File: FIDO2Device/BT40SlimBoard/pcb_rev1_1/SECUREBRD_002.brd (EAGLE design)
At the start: 30 x 30 mm, 31 parts, among them CN1 USB4105-GF-A, CN2 IF_5PIN_H, CN3 IF_2PIN_SOL, SW1 SKRPACE010, SW2 SKRPACE010, SW3 SKTADAE010, U1 BT40, U2 ADP122ACPZ-3.3-R7

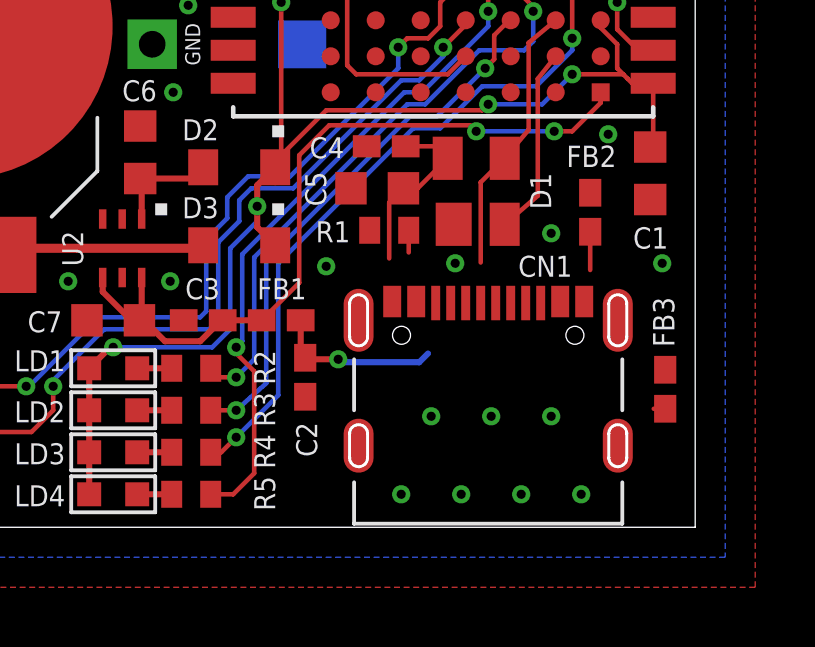
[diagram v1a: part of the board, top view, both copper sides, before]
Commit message: 配線レイアウトを修正
・部品入れ替えに伴い、配線レイアウトを修正
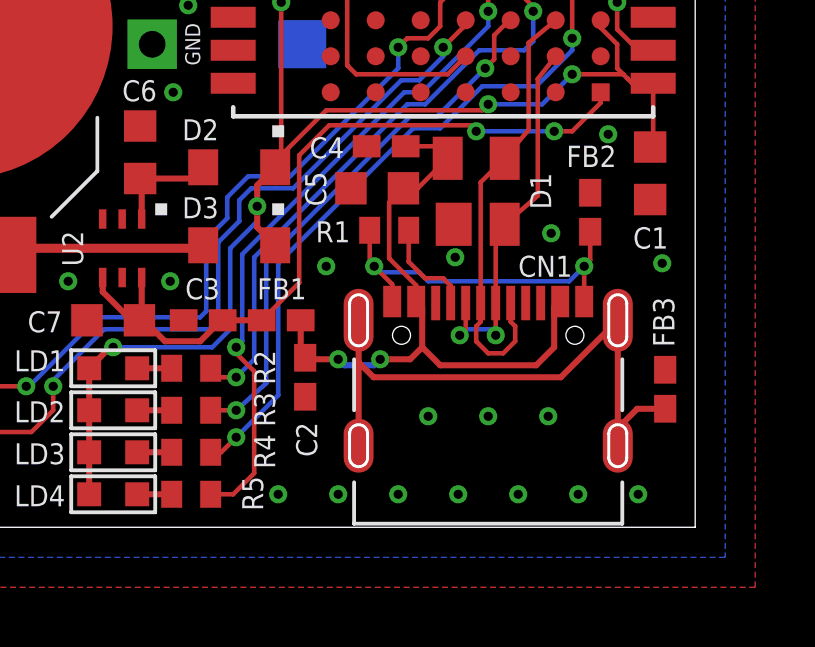
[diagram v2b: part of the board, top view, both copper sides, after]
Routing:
- net FG: track 0.38 -> 19.9 mm
- net USB_GND: track 1.27 -> 12.5 mm, vias 0 -> 2
- net VBUS: track 11.6 -> 21.6 mm, vias 1 -> 2
- net D_N: track 6.32 -> 12.7 mm, vias 0 -> 2
- net D_P: track 9.12 -> 14.8 mm
- net N$2: track 0.74 -> 3.36 mm
- net 0V: vias 18 -> 21
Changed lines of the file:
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@@
 </element>
 <element name="R5" library="Parts" package="R0402" value="390" x="13.2" y="1.1" smashed="yes" rot="R180">
-<attribute name="NAME" x="15.3" y="1.7" size="0.7" layer="25" rot="R270"/>
+<attribute name="NAME" x="14.9" y="1.7" size="0.7" layer="25" rot="R270"/>
 <attribute name="VALUE" x="13.755625" y="2.52875" size="0.7112" layer="27" rot="R180"/>
 </element>
@@
 <vertex x="-2" y="-2"/>
 </polygon>
-<via x="22" y="8.8" extent="1-16" drill="0.3048"/>
+<via x="22" y="9" extent="1-16" drill="0.3048"/>
 <via x="28.9" y="8.8" extent="1-16" drill="0.3048"/>
 <via x="27.4" y="17.5" extent="1-16" drill="0.3048"/>
@@
 <via x="17.7" y="8.7" extent="1-16" drill="0.3048"/>
 <via x="25.2" y="9.8" extent="1-16" drill="0.3048"/>
-<via x="22.2" y="1.1" extent="1-16" drill="0.3048"/>
-<via x="26.2" y="1.1" extent="1-16" drill="0.3048"/>
-<via x="20.2" y="1.1" extent="1-16" drill="0.3048"/>
-<via x="24.2" y="1.1" extent="1-16" drill="0.3048"/>
-<via x="23.2" y="3.7" extent="1-16" drill="0.3048"/>
-<via x="25.2" y="3.7" extent="1-16" drill="0.3048"/>
-<via x="21.2" y="3.7" extent="1-16" drill="0.3048"/>
+<via x="22.1" y="1.1" extent="1-16" drill="0.3048"/>
+<via x="26.1" y="1.1" extent="1-16" drill="0.3048"/>
+<via x="20.1" y="1.1" extent="1-16" drill="0.3048"/>
+<via x="24.1" y="1.1" extent="1-16" drill="0.3048"/>
+<via x="23.1" y="3.7" extent="1-16" drill="0.3048"/>
+<via x="25.1" y="3.7" extent="1-16" drill="0.3048"/>
+<via x="21.1" y="3.7" extent="1-16" drill="0.3048"/>
 <via x="27.1" y="13.1" extent="1-16" drill="0.3048"/>
 <via x="13.1" y="17.4" extent="1-16" drill="0.3048"/>
@@
 <via x="9.1" y="8.2" extent="1-16" drill="0.3048"/>
 <contactref element="CN3" pad="1"/>
+<via x="28.1" y="1.1" extent="1-16" drill="0.3048"/>
+<via x="18.1" y="1.1" extent="1-16" drill="0.3048"/>
+<via x="16.1" y="1.1" extent="1-16" drill="0.3048"/>
 </signal>
 <signal name="VBUS_NRF">
@@
 <wire x1="16.85" y1="5.8" x2="17" y2="5.65" width="0.2032" layer="1"/>
 <wire x1="17" y1="5.65" x2="17.05" y2="5.6" width="0.2032" layer="1"/>
-<wire x1="18.2" y1="5.5" x2="20.8" y2="5.5" width="0.2032" layer="16"/>
-<wire x1="20.8" y1="5.5" x2="21.0928" y2="5.7928" width="0.2032" layer="16"/>
 <wire x1="20.275" y1="11.3" x2="20.75" y2="11.3" width="0.1524" layer="1"/>
 <wire x1="20.75" y1="11.3" x2="21.75" y2="12.3" width="0.1524" layer="1"/>
@@
 <wire x1="21.35" y1="12.7" x2="21.75" y2="12.3" width="0.1524" layer="1"/>
 <wire x1="17.05" y1="5.6" x2="18.1" y2="5.6" width="0.2032" layer="1"/>
-<wire x1="18.2" y1="5.5" x2="18.1" y2="5.6" width="0.2032" layer="16"/>
 <contactref element="CN1" pad="A4"/>
 <contactref element="CN1" pad="B4"/>
-<wire x1="21.0928" y1="5.7928" x2="25.5" y2="7.525" width="0" layer="19" extent="1-16"/>
-<wire x1="20.7" y1="7.525" x2="21.0928" y2="5.7928" width="0" layer="19" extent="1-16"/>
-<wire x1="19.8" y1="8.9616" x2="20.7" y2="7.525" width="0" layer="19" extent="1-1"/>
+<via x="19.5" y="5.6" extent="1-16" drill="0.3048"/>
+<wire x1="19.4" y1="5.5" x2="19.5" y2="5.6" width="0.2032" layer="16"/>
+<wire x1="20.9" y1="7.325" x2="20.7" y2="7.525" width="0.1524" layer="1"/>
+<wire x1="20.7" y1="7.525" x2="20.7" y2="8.0616" width="0.1524" layer="1"/>
+<wire x1="20.7" y1="8.0616" x2="19.8" y2="8.9616" width="0.1524" layer="1"/>
+<wire x1="25.5" y1="7.525" x2="25.3" y2="7.325" width="0.2032" layer="1"/>
+<wire x1="25.3" y1="7.325" x2="25.3" y2="6" width="0.2032" layer="1"/>
+<wire x1="25.3" y1="6" x2="24.7" y2="5.4" width="0.2032" layer="1"/>
+<wire x1="20.9" y1="7.325" x2="20.9" y2="6" width="0.2032" layer="1"/>
+<wire x1="20.9" y1="6" x2="21.5" y2="5.4" width="0.2032" layer="1"/>
+<wire x1="21.5" y1="5.4" x2="24.7" y2="5.4" width="0.2032" layer="1"/>
+<wire x1="20.9" y1="6" x2="20.5" y2="5.6" width="0.2032" layer="1"/>
+<wire x1="20.5" y1="5.6" x2="19.5" y2="5.6" width="0.2032" layer="1"/>
+<wire x1="18.1" y1="5.6" x2="18.3" y2="5.4" width="0.2032" layer="16"/>
+<wire x1="18.3" y1="5.4" x2="19.3" y2="5.4" width="0.2032" layer="16"/>
+<wire x1="19.5" y1="5.6" x2="19.3" y2="5.4" width="0.2032" layer="16"/>
 </signal>
 <signal name="USB_GND">
 <contactref element="FB2" pad="1"/>
-<wire x1="26.5" y1="9.85" x2="26.5" y2="8.576" width="0.1524" layer="1"/>
 <contactref element="CN1" pad="B1"/>
 <contactref element="CN1" pad="A1"/>
 <contactref element="R1" pad="1"/>
-<wire x1="26.3" y1="7.525" x2="26.5" y2="8.576" width="0" layer="19" extent="1-1"/>
-<wire x1="19.9" y1="7.525" x2="26.3" y2="7.525" width="0" layer="19" extent="1-1"/>
-<wire x1="19.15" y1="9.9" x2="19.9" y2="7.525" width="0" layer="19" extent="1-1"/>
+<via x="19.3" y="8.7" extent="1-16" drill="0.3048"/>
+<wire x1="19.15" y1="9.9" x2="19.15" y2="8.85" width="0.1524" layer="1"/>
+<wire x1="19.15" y1="8.85" x2="19.3" y2="8.7" width="0.1524" layer="1"/>
+<wire x1="19.9" y1="7.525" x2="19.9" y2="8.1" width="0.1524" layer="1"/>
+<wire x1="19.9" y1="8.1" x2="19.3" y2="8.7" width="0.1524" layer="1"/>
+<via x="26.3" y="8.7" extent="1-16" drill="0.3048"/>
+<wire x1="26.3" y1="7.525" x2="26.3" y2="8.7" width="0.1524" layer="1"/>
+<wire x1="26.5" y1="9.85" x2="26.5" y2="8.9" width="0.1524" layer="1"/>
+<wire x1="26.5" y1="8.9" x2="26.3" y2="8.7" width="0.1524" layer="1"/>
+<wire x1="26.3" y1="8.7" x2="25.8" y2="8.2" width="0.1524" layer="16"/>
+<wire x1="25.8" y1="8.2" x2="21.1" y2="8.2" width="0.1524" layer="16"/>
+<wire x1="21.1" y1="8.2" x2="20.8" y2="8.5" width="0.1524" layer="16"/>
+<wire x1="20.8" y1="8.5" x2="19.5" y2="8.5" width="0.1524" layer="16"/>
+<wire x1="19.5" y1="8.5" x2="19.3" y2="8.7" width="0.1524" layer="16"/>
 </signal>
 <signal name="FG">
 <contactref element="FB3" pad="1"/>
-<wire x1="29" y1="3.95" x2="28.619" y2="3.95" width="0.1524" layer="1"/>
 <contactref element="CN1" pad="FG4"/>
 <contactref element="CN1" pad="FG3"/>
 <contactref element="CN1" pad="FG1"/>
 <contactref element="CN1" pad="FG2"/>
-<wire x1="27.42" y1="2.72" x2="28.619" y2="3.95" width="0" layer="19" extent="1-1"/>
-<wire x1="27.42" y1="6.9" x2="28.619" y2="3.95" width="0" layer="19" extent="1-1"/>
-<wire x1="18.78" y1="6.9" x2="27.42" y2="6.9" width="0" layer="19" extent="1-1"/>
-<wire x1="18.78" y1="2.72" x2="18.78" y2="6.9" width="0" layer="19" extent="1-1"/>
+<wire x1="18.78" y1="6.9" x2="18.78" y2="5.5" width="0.2032" layer="1"/>
+<wire x1="18.78" y1="5.5" x2="18.78" y2="2.72" width="0.2032" layer="1"/>
+<wire x1="27.42" y1="6.9" x2="27.42" y2="3.3" width="0.2032" layer="1"/>
+<wire x1="27.42" y1="3.3" x2="27.42" y2="2.72" width="0.2032" layer="1"/>
+<wire x1="18.78" y1="6.9" x2="18.78" y2="6.82" width="0.2032" layer="1"/>
+<wire x1="25.52" y1="5" x2="27.42" y2="6.9" width="0.2032" layer="1"/>
+<wire x1="29" y1="3.95" x2="28.07" y2="3.95" width="0.2032" layer="1"/>
+<wire x1="28.07" y1="3.95" x2="27.42" y2="3.3" width="0.2032" layer="1"/>
+<wire x1="25.52" y1="5" x2="19.28" y2="5" width="0.2032" layer="1"/>
+<wire x1="19.28" y1="5" x2="18.78" y2="5.5" width="0.2032" layer="1"/>
 </signal>
 <signal name="D_N">
@@
 <contactref element="CN1" pad="A7"/>
 <contactref element="CN1" pad="B7"/>
-<wire x1="23.35" y1="7.475" x2="23.6428" y2="10.0928" width="0" layer="19" extent="1-1"/>
-<wire x1="22.35" y1="7.475" x2="23.35" y2="7.475" width="0" layer="19" extent="1-1"/>
+<wire x1="23.35" y1="7.475" x2="23.35" y2="9.8" width="0.1524" layer="1"/>
+<wire x1="23.35" y1="9.8" x2="23.65" y2="10.1" width="0.1524" layer="1"/>
+<via x="23.35" y="6.4" extent="1-16" drill="0.3048"/>
+<via x="22.15" y="6.4" extent="1-16" drill="0.3048"/>
+<wire x1="23.35" y1="7.475" x2="23.35" y2="6.4" width="0.1524" layer="1"/>
+<wire x1="22.35" y1="7.475" x2="22.35" y2="6.6" width="0.1524" layer="1"/>
+<wire x1="22.35" y1="6.6" x2="22.15" y2="6.4" width="0.1524" layer="1"/>
+<wire x1="22.15" y1="6.4" x2="22.35" y2="6.6" width="0.1524" layer="16"/>
+<wire x1="23.35" y1="6.4" x2="23.15" y2="6.6" width="0.1524" layer="16"/>
+<wire x1="23.15" y1="6.6" x2="22.35" y2="6.6" width="0.1524" layer="16"/>
 </signal>
 <signal name="D_P">
@@
 <wire x1="23.65" y1="12.3" x2="24.4476" y2="13.25" width="0.1524" layer="1"/>
 <wire x1="23.65" y1="12.3" x2="22.85" y2="11.5" width="0.1524" layer="1"/>
-<wire x1="22.85" y1="11.5" x2="22.85" y2="8.826" width="0.1524" layer="1"/>
 <contactref element="CN1" pad="A6"/>
 <contactref element="CN1" pad="B6"/>
-<wire x1="22.85" y1="7.475" x2="22.85" y2="8.826" width="0" layer="19" extent="1-1"/>
-<wire x1="23.85" y1="7.475" x2="22.85" y2="7.475" width="0" layer="19" extent="1-1"/>
+<wire x1="22.85" y1="11.5" x2="22.85" y2="7.475" width="0.1524" layer="1"/>
+<wire x1="22.85" y1="7.475" x2="22.85" y2="6.85" width="0.1524" layer="1"/>
+<wire x1="22.85" y1="6.85" x2="22.7" y2="6.7" width="0.1524" layer="1"/>
+<wire x1="22.7" y1="6.7" x2="22.7" y2="6.2" width="0.1524" layer="1"/>
+<wire x1="22.7" y1="6.2" x2="23.1" y2="5.8" width="0.1524" layer="1"/>
+<wire x1="23.1" y1="5.8" x2="23.6" y2="5.8" width="0.1524" layer="1"/>
+<wire x1="23.85" y1="7.475" x2="23.85" y2="6.85" width="0.1524" layer="1"/>
+<wire x1="23.85" y1="6.85" x2="24" y2="6.7" width="0.1524" layer="1"/>
+<wire x1="24" y1="6.7" x2="24" y2="6.2" width="0.1524" layer="1"/>
+<wire x1="24" y1="6.2" x2="23.6" y2="5.8" width="0.1524" layer="1"/>
 </signal>
 <signal name="LED2">
@@
 <signal name="N$2">
 <contactref element="R1" pad="2"/>
-<wire x1="20.45" y1="9.1616" x2="20.45" y2="9.9" width="0.1524" layer="1"/>
+<wire x1="20.45" y1="8.85" x2="20.45" y2="9.9" width="0.1524" layer="1"/>
 <contactref element="CN1" pad="A5"/>
-<wire x1="21.85" y1="7.475" x2="20.45" y2="9.1616" width="0" layer="19" extent="1-1"/>
+<wire x1="21" y1="8.3" x2="20.45" y2="8.85" width="0.1524" layer="1"/>
+<wire x1="21.85" y1="7.475" x2="21.85" y2="8.05" width="0.1524" layer="1"/>
+<wire x1="21.85" y1="8.05" x2="21.6" y2="8.3" width="0.1524" layer="1"/>
+<wire x1="21.6" y1="8.3" x2="21" y2="8.3" width="0.1524" layer="1"/>
 </signal>
 <signal name="N$3">
